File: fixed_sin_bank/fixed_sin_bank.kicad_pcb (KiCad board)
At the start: 2 copper layers, 18.8 x 116.8 mm, 101 parts, among them J101 Conn_02x05_Odd_Even, J201 AudioJack2_SwitchT, J301 AudioJack2_SwitchT, J401 AudioJack2_SwitchT, J501 AudioJack2_SwitchT, J601 AudioJack2_SwitchT, J701 AudioJack2_SwitchT, U201 TL071HDBV, U301 TL071HDBV, U401 TL071HDBV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

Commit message: First draft of pcb
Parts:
- moved R505 1.26 mm to (134.5, 104.2)
- moved R305 1.26 mm to (134.5, 70.7)
- moved R405 1.26 mm to (134.5, 87.4)
- moved R605 1.26 mm to (134.5, 121.0)
- moved R705 1.26 mm to (134.5, 137.7)
- moved R205 1.26 mm to (134.5, 53.9)
- moved R407 0.46 mm to (146.4, 80.5)
- moved R507 0.46 mm to (146.4, 97.3)
- moved R307 0.46 mm to (146.4, 63.8)
- moved R607 0.46 mm to (146.4, 114.1)
- moved R707 0.46 mm to (146.4, 130.8)
- moved R207 0.46 mm to (146.4, 47.0)
- moved D102 0.24 mm to (150.1, 35.6)
- moved D101 0.17 mm to (133.9, 35.6)
- turned C101 to 0 degrees
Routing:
- net VEE: track 91.0 -> 200.4 mm
- net VCC: track 133.0 -> 150.6 mm
- net GND: track 77.5 -> 86.5 mm
- net Net-(R203-Pad2): track 26.4 -> 28.6 mm
- net Net-(R303-Pad2): track 26.4 -> 28.6 mm
- net Net-(R603-Pad2): track 26.4 -> 28.6 mm
- net Net-(R403-Pad2): track 26.4 -> 28.6 mm
- net Net-(R503-Pad2): track 26.4 -> 28.6 mm
- net Net-(R703-Pad2): track 26.4 -> 28.6 mm
- net Net-(D702-K): track 2.62 -> 3.92 mm
- net Net-(D502-K): track 2.62 -> 3.92 mm
- net Net-(D302-K): track 2.62 -> 3.92 mm
- net Net-(D202-K): track 2.62 -> 3.92 mm
- net Net-(D402-K): track 2.62 -> 3.92 mm
- net Net-(D602-K): track 2.62 -> 3.92 mm
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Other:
- board text added: "fixed sin bank v1.0 www.birchavenue.org"

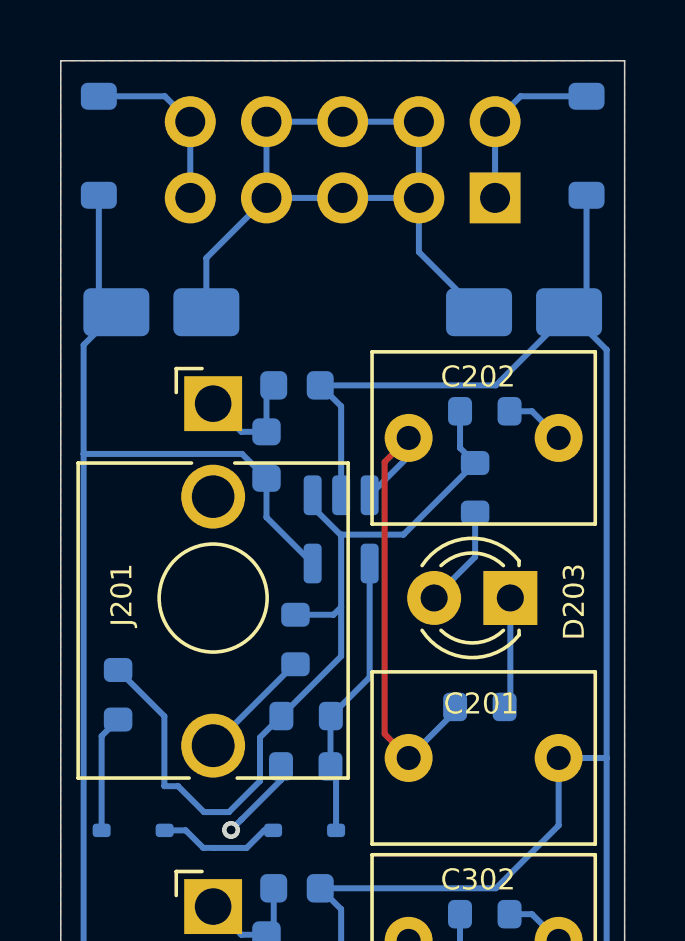
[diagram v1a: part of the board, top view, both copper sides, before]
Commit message: Add polarity warning to pcb
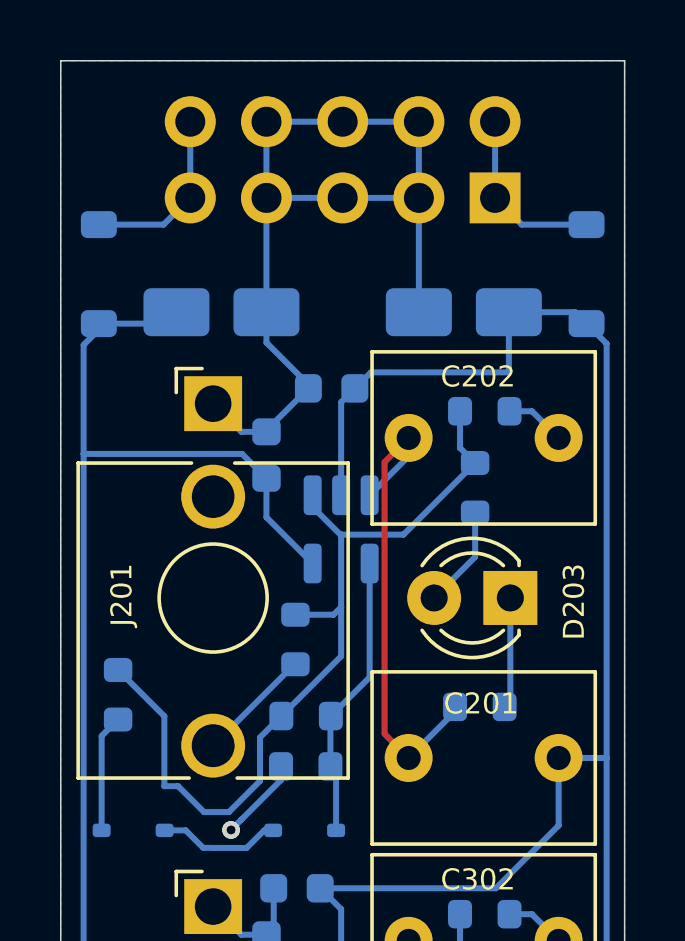
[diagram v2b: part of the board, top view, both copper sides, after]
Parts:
- moved D101 4.28 mm to (133.9, 39.9)
- moved D102 4.28 mm to (150.1, 39.9)
- moved C101 2.01 mm to (137.9, 41.1)
- moved C102 2.01 mm to (146.0, 41.1)
- moved C204 1.16 mm to (141.6, 43.7)
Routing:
- net VEE: track 200.4 -> 196.4 mm
- net VCC: track 150.6 -> 148.5 mm
- net GND: track 86.5 -> 88.4 mm
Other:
- board text added: "Red"
